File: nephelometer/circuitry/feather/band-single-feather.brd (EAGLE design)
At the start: 95 x 55 mm, 72 parts, among them IC1 LP2950ACZ-3.3, IC2 LM4041CILP, IC3 AD822N, IC4 7805TV, IC5 MCP6S21, IC6 MAX144, IC7 FEATHER_M0, J1 PJ-102A, J2 MotA, J3 MotA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

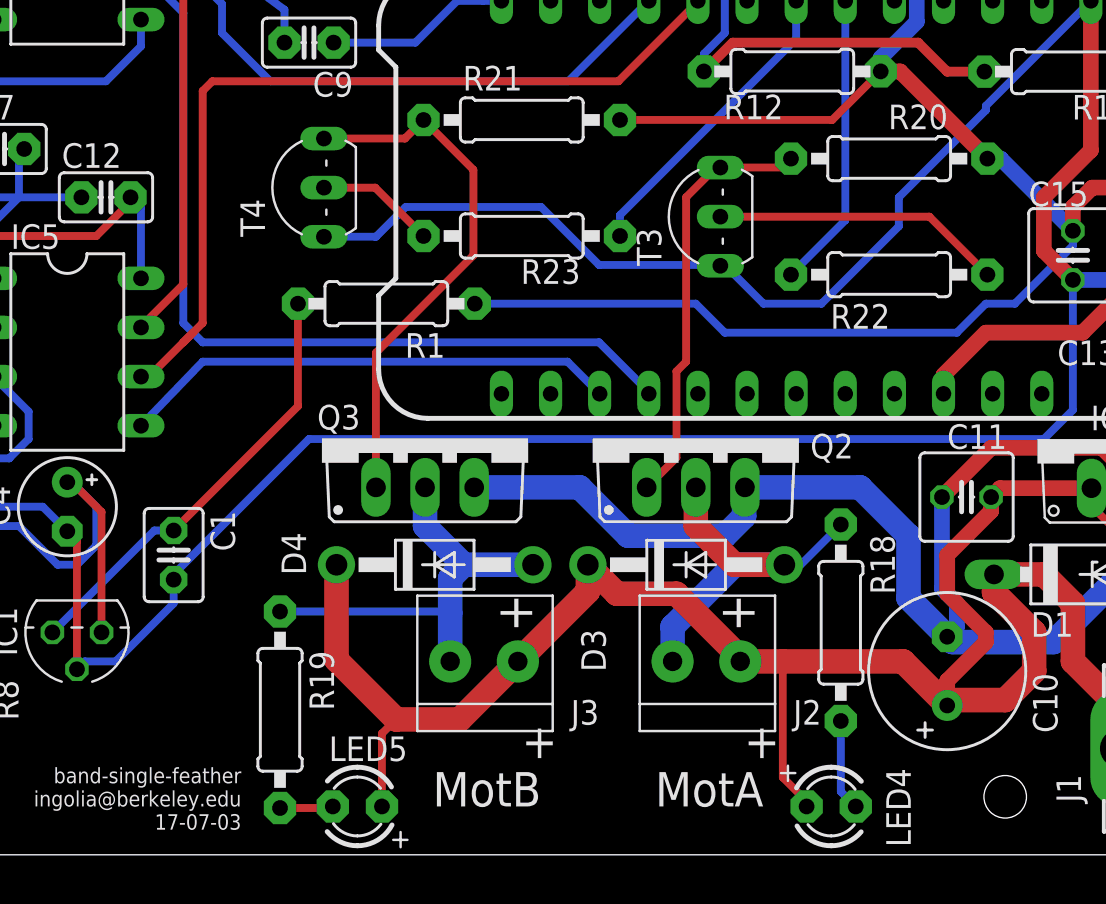
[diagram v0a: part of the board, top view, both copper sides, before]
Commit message: Pullup resistor to shut off motors during startup with high-Z pin on microcontroller. Replaced obsolete flyback diode.
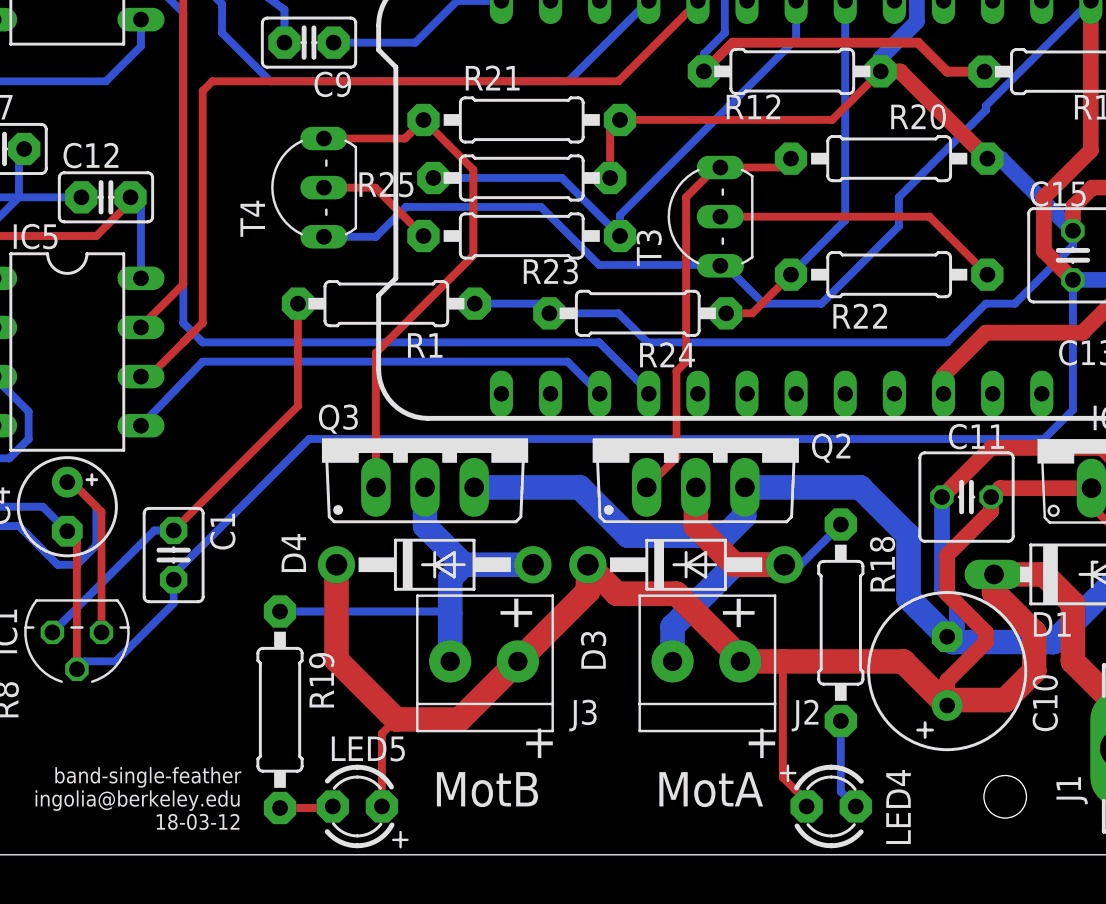
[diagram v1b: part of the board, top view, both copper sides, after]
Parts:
- added R24, R25: 33k, adafruit:0207/9
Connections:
- net +5V: now also R24.2, R25.2
- net MOT1_CTRL: now also R24.1
- net MOT2_CTRL: now also R25.1
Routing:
- net MOT2_CTRL: track 15.9 -> 26.8 mm
- net MOT1_CTRL: track 15.3 -> 19.5 mm
- net +5V: track 120.2 -> 123.9 mm
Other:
- board text added: "band-single-feather ingolia@berkeley.edu 18-03-12"
- board text removed: "band-single-feather ingolia@berkeley.edu 17-07-03"
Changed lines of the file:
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@@
 <text x="37.5" y="9.5" size="0.8" layer="21" font="vector" rot="R180">band-single-feather
 ingolia@berkeley.edu
-17-07-03</text>
+18-03-12</text>
 <text x="91.5" y="16.5" size="0.5" layer="21" rot="R90">VIN</text>
 <wire x1="0.5" y1="24.3" x2="3.8" y2="30" width="0.25" layer="29"/>
@@
 </element>
 <element name="D3" library="adafruit" package="DO41-10" value="1N4935" x="60.5" y="20" smashed="yes">
-<attribute name="DIGIKEY#" value="1N4935FSCT-ND" x="60.5" y="-19.5" size="1.778" layer="27" display="off"/>
-<attribute name="MANF" value="Fairchild Semiconductor" x="60.5" y="-19.5" size="1.778" layer="27" display="off"/>
-<attribute name="MANF#" value="1N4935" x="60.5" y="-19.5" size="1.778" layer="27" display="off"/>
+<attribute name="DIGIKEY#" value="1N4935GOS-ND" x="60.5" y="-19.5" size="1.778" layer="27" display="off"/>
+<attribute name="MANF" value="ON Semiconductor" x="60.5" y="-19.5" size="1.778" layer="27" display="off"/>
+<attribute name="MANF#" value="1N4935G" x="60.5" y="-19.5" size="1.778" layer="27" display="off"/>
 <attribute name="NAME" x="56.349" y="14.468" size="1.27" layer="25" ratio="10" rot="R90"/>
 <attribute name="VALUE" x="58.468" y="17.206" size="1.27" layer="27" ratio="10"/>
@@
 </element>
 <element name="D4" library="adafruit" package="DO41-10" value="1N4935" x="47.5" y="20" smashed="yes">
-<attribute name="DIGIKEY#" value="1N4935FSCT-ND" x="47.5" y="-19.5" size="1.778" layer="27" display="off"/>
-<attribute name="MANF" value="Fairchild Semiconductor" x="47.5" y="-19.5" size="1.778" layer="27" display="off"/>
-<attribute name="MANF#" value="1N4935" x="47.5" y="-19.5" size="1.778" layer="27" display="off"/>
+<attribute name="DIGIKEY#" value="1N4935GOS-ND" x="47.5" y="-19.5" size="1.778" layer="27" display="off"/>
+<attribute name="MANF" value="ON Semiconductor" x="47.5" y="-19.5" size="1.778" layer="27" display="off"/>
+<attribute name="MANF#" value="1N4935G" x="47.5" y="-19.5" size="1.778" layer="27" display="off"/>
 <attribute name="NAME" x="40.849" y="19.468" size="1.27" layer="25" ratio="10" rot="R90"/>
 <attribute name="VALUE" x="45.468" y="17.206" size="1.27" layer="27" ratio="10"/>
@@
 <attribute name="NAME" x="82.786" y="31.595" size="1.27" layer="25" ratio="10" rot="R180"/>
 <attribute name="VALUE" x="87.786" y="33.048" size="1.27" layer="27" ratio="10" rot="R180"/>
+</element>
+<element name="R24" library="adafruit" package="0207/9" value="33k" x="58" y="33" rot="R180">
+<attribute name="DIGIKEY#" value="CF14JT33K0CT-ND" x="58" y="33" size="1.778" layer="27" rot="R180" display="off"/>
+<attribute name="MANF" value="Stackpole Electronics Inc" x="58" y="33" size="1.778" layer="27" rot="R180" display="off"/>
+<attribute name="MANF#" value="CF14JT33K0" x="58" y="33" size="1.778" layer="27" rot="R180" display="off"/>
+</element>
+<element name="R25" library="adafruit" package="0207/9" value="33k" x="52" y="40" smashed="yes">
+<attribute name="DIGIKEY#" value="CF14JT33K0CT-ND" x="52" y="40" size="1.778" layer="27" display="off"/>
+<attribute name="MANF" value="Stackpole Electronics Inc" x="52" y="40" size="1.778" layer="27" display="off"/>
+<attribute name="MANF#" value="CF14JT33K0" x="52" y="40" size="1.778" layer="27" display="off"/>
+<attribute name="NAME" x="43.452" y="39.024" size="1.27" layer="25" ratio="10"/>
+<attribute name="VALUE" x="49.7394" y="39.365" size="1.27" layer="27" ratio="10"/>
 </element>
 </elements>
@@
 <wire x1="57.08" y1="43" x2="68.052" y2="43" width="0.4064" layer="1"/>
 <wire x1="68.052" y1="43" x2="70.562" y2="45.51" width="0.4064" layer="1"/>
-<wire x1="49.572" y1="33.5" x2="61" y2="33.5" width="0.4064" layer="16"/>
-<wire x1="61" y1="33.5" x2="62.5" y2="32" width="0.4064" layer="16"/>
 <contactref element="C14" pad="1"/>
 <contactref element="C15" pad="1"/>
@@
 <wire x1="76.08" y1="41" x2="76.77" y2="41" width="0.8128" layer="16"/>
 <wire x1="80.5" y1="37.27" x2="76.77" y2="41" width="0.8128" layer="16"/>
-<wire x1="62.5" y1="32" x2="74.5" y2="32" width="0.4064" layer="16"/>
-<wire x1="74.5" y1="32" x2="76" y2="33.5" width="0.4064" layer="16"/>
+<wire x1="74" y1="31.5" x2="76" y2="33.5" width="0.4064" layer="16"/>
 <wire x1="76" y1="33.5" x2="77.5" y2="33.5" width="0.4064" layer="16"/>
 <wire x1="77.5" y1="33.5" x2="80.5" y2="36.5" width="0.4064" layer="16"/>
 <wire x1="80.5" y1="36.5" x2="80.5" y2="37.27" width="0.4064" layer="16"/>
+<contactref element="R24" pad="2"/>
+<contactref element="R25" pad="2"/>
+<wire x1="58.5" y1="31.5" x2="74" y2="31.5" width="0.4064" layer="16"/>
+<wire x1="49.572" y1="33.5" x2="52.928" y2="33.5" width="0.4064" layer="16"/>
+<wire x1="52.928" y1="33.5" x2="53.428" y2="33" width="0.4064" layer="16"/>
+<wire x1="53.428" y1="33" x2="57" y2="33" width="0.4064" layer="16"/>
+<wire x1="57" y1="33" x2="58.5" y2="31.5" width="0.4064" layer="16"/>
+<wire x1="56.572" y1="40" x2="56.572" y2="42.492" width="0.4064" layer="1"/>
+<wire x1="56.572" y1="42.492" x2="57.08" y2="43" width="0.4064" layer="1"/>
 </signal>
 <signal name="VBAT">
@@
 <wire x1="68.73" y1="49.16" x2="68.73" y2="37.81" width="0.4064" layer="16"/>
 <wire x1="68.73" y1="37.81" x2="65.92" y2="35" width="0.4064" layer="16"/>
+<contactref element="R24" pad="1"/>
+<wire x1="62.572" y1="33" x2="63.92" y2="33" width="0.4064" layer="1"/>
+<wire x1="63.92" y1="33" x2="65.92" y2="35" width="0.4064" layer="1"/>
 </signal>
 <signal name="VDD">
@@
 <contactref element="IC7" pad="P$19"/>
 <contactref element="R23" pad="2"/>
-<wire x1="57.08" y1="38.08" x2="57.08" y2="37" width="0.4064" layer="16"/>
+<wire x1="57.08" y1="37" x2="57.08" y2="38.08" width="0.4064" layer="16"/>
 <wire x1="66.19" y1="49.16" x2="66.19" y2="47.19" width="0.4064" layer="16"/>
 <wire x1="66.19" y1="47.19" x2="57.08" y2="38.08" width="0.4064" layer="16"/>
+<contactref element="R25" pad="1"/>
+<wire x1="47.428" y1="40" x2="54.08" y2="40" width="0.4064" layer="16"/>
+<wire x1="54.08" y1="40" x2="57.08" y2="37" width="0.4064" layer="16"/>
 </signal>
 <signal name="MOT3_CTRL">
